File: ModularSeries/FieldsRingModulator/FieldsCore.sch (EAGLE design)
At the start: 37 parts

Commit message: Fields added and various updates to designs
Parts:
- removed C3, C4: 220nF, rcl:C-EU050-025X075
- removed C5, C6, C8, C9: 100nF, rcl:C-EU050-025X075
- removed C7: 22pF, rcl:C-EU050-025X075
- removed GNDT: 4XWIREPAD, ElectricNoodleBox:4XWIREPAD
- removed H3, H4: MOUNT-HOLE3.2, holes:MOUNT-HOLE3.2
- removed HPVOL, MSTR: A100K, ElectricNoodleBox:2XWIREPAD
- removed HP_OUT, HP_OUT1: 3XWIREPAD, ElectricNoodleBox:3XWIREPAD
- removed IC2: (no value), ElectricNoodleBox:TL0X2DIL
- removed IN1, IN2, IN3, IN4: B100K, ElectricNoodleBox:1XWIREPAD
- removed R10, R9: 75Ω, rcl:R-EU_0207/10
- removed R11: 1K, rcl:R-EU_0207/10
- removed R6, R7: 100K, rcl:R-EU_0207/10
- removed R8: 12K, rcl:R-EU_0207/10
- added CAR, IN, OUT: 1XWIREPAD, ElectricNoodleBox:1XWIREPAD
- added D1, D2, D3, D4: (no value), diode:DIODE-DO35-10
- added GND, POT: 2XWIREPAD, ElectricNoodleBox:2XWIREPAD
- added Z2: (no value), ElectricNoodleBox:Z1604_AUDIO_TRANSFORMER
- C1, C2: value 220nF -> 100nF
- H1, H2: value MOUNT-HOLE3.2 -> MOUNT-PAD-ROUND3.2; device holes:MOUNT-HOLE3.2 -> holes:MOUNT-PAD-ROUND3.2
- R1, R2, R3, R4: value 100K -> 10K
- R5: value 47K -> 100Ω
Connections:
- removed net HP_VOLOUT: HPVOL.2, IC2A.+IN, IC2B.+IN
- removed net N$15: HP_OUT1.1, Z1.6
- removed net N$16: HP_OUT1.2, Z1.5
- removed net N$17: HP_OUT1.3, Z1.4
- removed net N$18: IC2A.-IN, IC2A.OUT, R9.1
- removed net N$19: HP_OUT.1, R9.2
- removed net N$20: IC2B.-IN, IC2B.OUT, R10.1
- removed net N$21: HP_OUT.2, R10.2
- removed net N$22: R11.2, Z1.1
- removed net N$9: C2.2, R2.1
- net +12V: now also C1.1; no longer C5.1, C8.1, IC2P.V+
- net -12V: now also C2.2; no longer C6.2, C9.2, IC2P.V-
- net AGND: now also C1.2, C2.1, GND.1, GND.2, IC1A.+IN, Z2.3, Z2.5; no longer C5.2, C6.1, C8.2, C9.1, GNDT.1, GNDT.2, GNDT.3, GNDT.4, HP_OUT.3, R6.2
- net N$1: now also D1.A, D4.C, Z1.6; no longer C4.1, IN4.1
- net N$10: now also POT.1, R2.2; no longer C3.2, R3.1
- net N$11: now also IC1A.OUT, POT.2, R3.1; no longer C4.2, R4.1
- net N$12: now also IC1B.-IN, R3.2, R4.1; no longer C2.1, IN2.1
- net N$13: now also IC1B.OUT, R4.2, R5.1; no longer C1.1, IN1.1
- net N$14: now also OUT.1, R5.2; no longer MSTR.2, R11.1
- net N$2: now also D1.C, D2.A, Z2.6; no longer C7.1, IC1A.-IN, R1.2, R2.2, R3.2, R4.2, R5.2
- net N$3: now also D2.C, D3.A, Z1.4; no longer C7.2, IC1A.OUT, R5.1, R7.1
- net N$4: now also D3.C, D4.A, Z2.4; no longer IC1B.-IN, R7.2, R8.1
- net N$5: now also CAR.1, Z1.5; no longer HPVOL.1, IC1B.OUT, MSTR.1, R8.2
- net N$6: now also R1.1, Z2.1; no longer C3.1, IN3.1
- net N$7: now also IC1A.-IN, R1.2, R2.1; no longer IC1A.+IN, R6.1
- net N$8: now also IN.1, Z1.1; no longer C1.2, R1.1
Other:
- note added: "B100K"
- note added: "R1 and R2 might need to be higher e.g. 22K"
- note added: "Recommended 1N34, 1N270 or BAT85 for D1, 2, 3 and 4"
- note removed: "1 - In phase 2 - GND 3 - Out of phase Only use 3 for balanced output, use 1 and 2 only for unbalanced"
- note removed: "Endings: AC Mixer and Isolated Output Aidan Taylor 2020 ELECTRIC NOODLE BOX"
- note removed: "Headphone Driver to TRS Minijack"
- moved on the sheet: C1, C2, H1, H2, IC1A, IC1B, IC1P, R1, R2, R3, R4, R5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

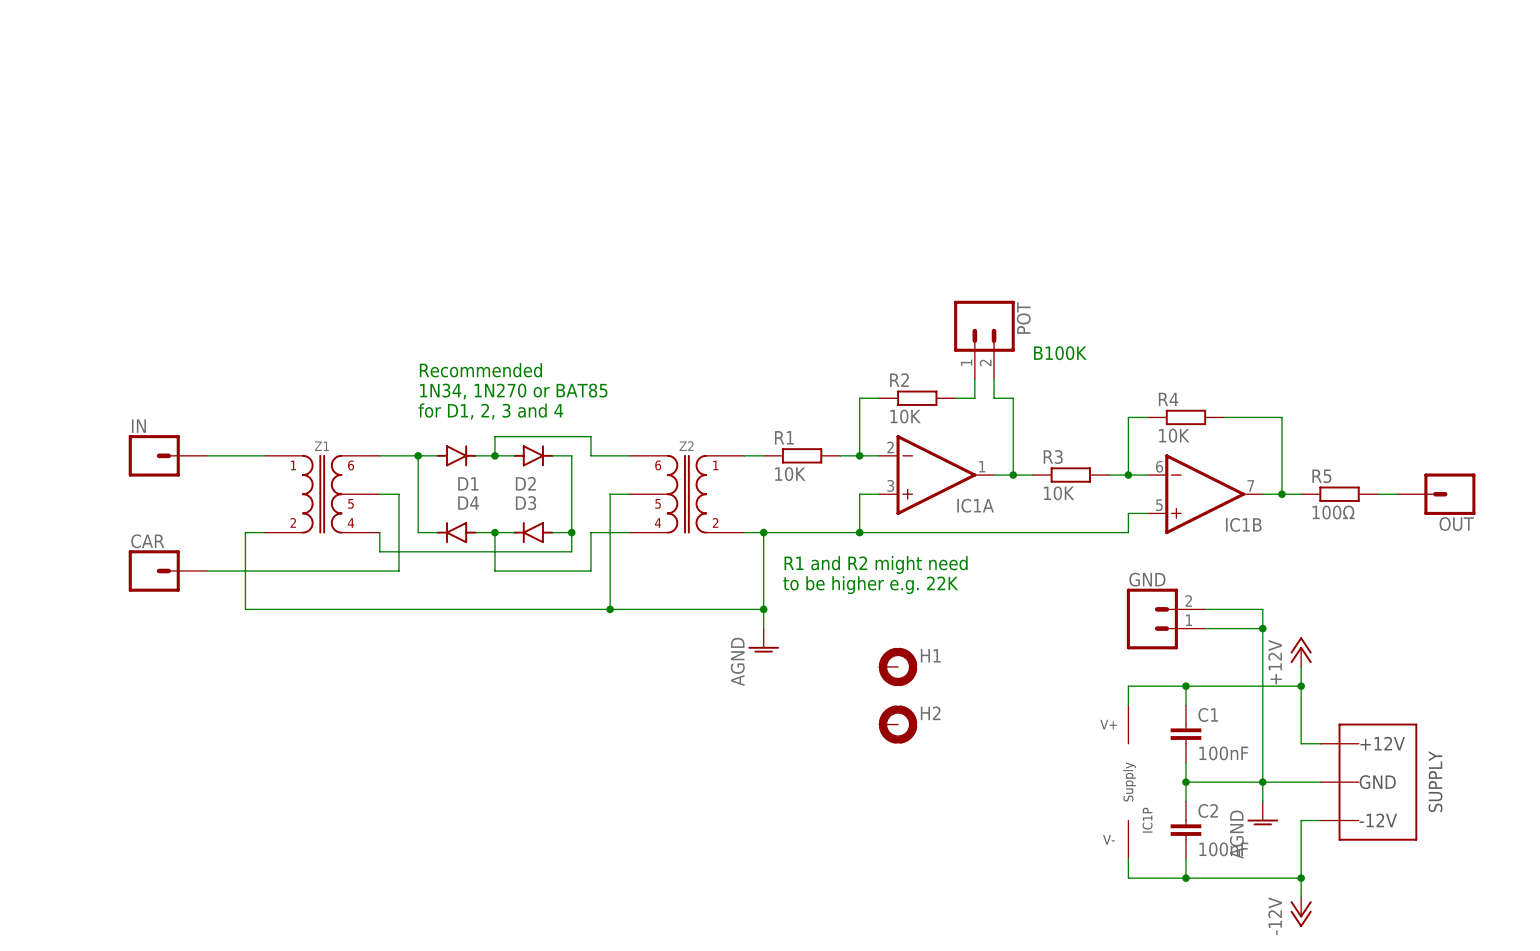
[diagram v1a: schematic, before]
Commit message: Fields module images and BOM added
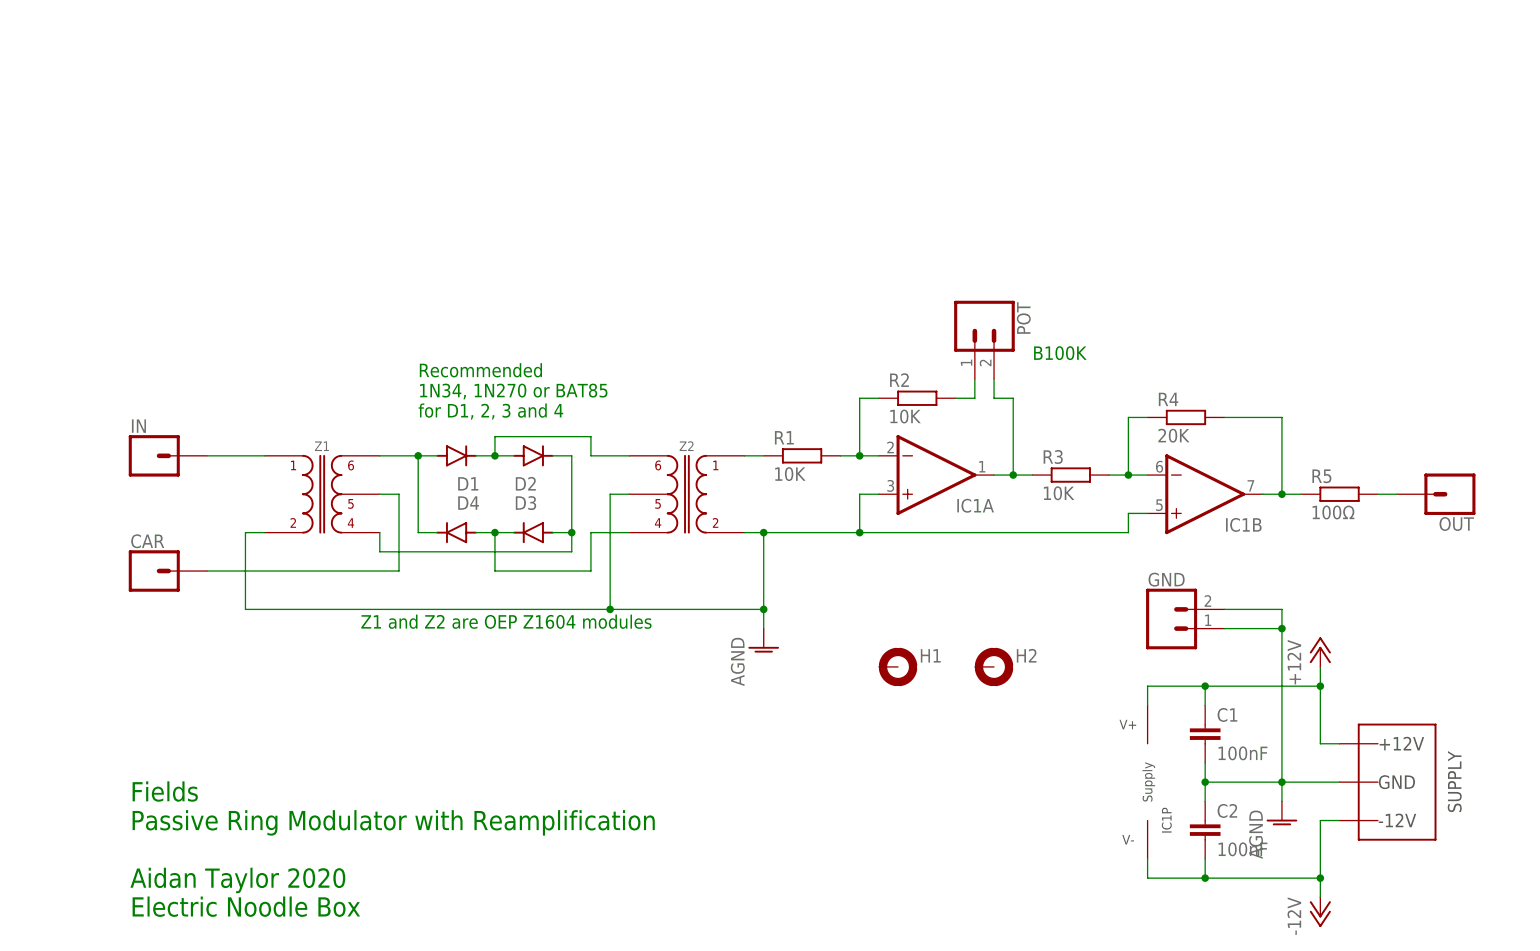
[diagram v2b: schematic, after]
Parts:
- R4: value 10K -> 20K
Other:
- note added: "Fields Passive Ring Modulator with Reamplification Aidan Taylor 2020 Electric Noodle Box"
- note added: "Z1 and Z2 are OEP Z1604 modules"
- note removed: "R1 and R2 might need to be higher e.g. 22K"
- moved on the sheet: C1, C2, GND, H2, IC1P
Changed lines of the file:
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@@
 <part name="POT" library="ElectricNoodleBox" deviceset="2XWIREPAD" device=""/>
 <part name="R3" library="rcl" library_urn="urn:adsk.eagle:library:334" deviceset="R-EU_" device="0207/10" package3d_urn="urn:adsk.eagle:package:23491/2" value="10K"/>
-<part name="R4" library="rcl" library_urn="urn:adsk.eagle:library:334" deviceset="R-EU_" device="0207/10" package3d_urn="urn:adsk.eagle:package:23491/2" value="10K"/>
+<part name="R4" library="rcl" library_urn="urn:adsk.eagle:library:334" deviceset="R-EU_" device="0207/10" package3d_urn="urn:adsk.eagle:package:23491/2" value="20K"/>
 <part name="R5" library="rcl" library_urn="urn:adsk.eagle:library:334" deviceset="R-EU_" device="0207/10" package3d_urn="urn:adsk.eagle:package:23491/2" value="100Ω"/>
 <part name="P+1" library="supply1" library_urn="urn:adsk.eagle:library:371" deviceset="+12V" device=""/>
@@
 1N34, 1N270 or BAT85
 for D1, 2, 3 and 4</text>
-<text x="93.98" y="38.1" size="1.778" layer="91">R1 and R2 might need
-to be higher e.g. 22K</text>
 <text x="127" y="68.58" size="1.778" layer="91">B100K </text>
+<text x="38.1" y="33.02" size="1.778" layer="91">Z1 and Z2 are OEP Z1604 modules</text>
+<text x="7.62" y="-5.08" size="2.54" layer="91">Fields
+Passive Ring Modulator with Reamplification
+Aidan Taylor 2020
+Electric Noodle Box</text>
 </plain>
 <instances>
@@
 <attribute name="NAME" x="152.4" y="47.625" size="1.778" layer="95" rot="MR180"/>
 </instance>
-<instance part="IC1" gate="P" x="139.7" y="12.7" smashed="yes">
-<attribute name="NAME" x="142.24" y="7.62" size="1.27" layer="97" rot="R90" align="center"/>
-</instance>
-<instance part="WP1" gate="G$1" x="172.72" y="12.7" smashed="yes"/>
+<instance part="IC1" gate="P" x="142.24" y="12.7" smashed="yes">
+<attribute name="NAME" x="144.78" y="7.62" size="1.27" layer="97" rot="R90" align="center"/>
+</instance>
+<instance part="WP1" gate="G$1" x="175.26" y="12.7" smashed="yes"/>
 <instance part="R1" gate="G$1" x="96.52" y="55.88" smashed="yes">
 <attribute name="NAME" x="92.71" y="57.3786" size="1.778" layer="95"/>
@@
 <attribute name="VALUE" x="163.83" y="47.498" size="1.778" layer="96"/>
 </instance>
-<instance part="P+1" gate="1" x="162.56" y="30.48" smashed="yes">
-<attribute name="VALUE" x="160.02" y="25.4" size="1.778" layer="96" rot="R90"/>
-</instance>
-<instance part="P-1" gate="1" x="162.56" y="-5.08" smashed="yes">
-<attribute name="VALUE" x="160.02" y="-7.62" size="1.778" layer="96" rot="R90"/>
-</instance>
-<instance part="AGND1" gate="VR1" x="157.48" y="7.62" smashed="yes">
-<attribute name="VALUE" x="154.94" y="2.54" size="1.778" layer="96" rot="R90"/>
-</instance>
-<instance part="C1" gate="G$1" x="147.32" y="20.32" smashed="yes">
-<attribute name="NAME" x="148.844" y="20.701" size="1.778" layer="95"/>
-<attribute name="VALUE" x="148.844" y="15.621" size="1.778" layer="96"/>
-</instance>
-<instance part="C2" gate="G$1" x="147.32" y="7.62" smashed="yes">
-<attribute name="NAME" x="148.844" y="8.001" size="1.778" layer="95"/>
-<attribute name="VALUE" x="148.844" y="2.921" size="1.778" layer="96"/>
+<instance part="P+1" gate="1" x="165.1" y="30.48" smashed="yes">
+<attribute name="VALUE" x="162.56" y="25.4" size="1.778" layer="96" rot="R90"/>
+</instance>
+<instance part="P-1" gate="1" x="165.1" y="-5.08" smashed="yes">
+<attribute name="VALUE" x="162.56" y="-7.62" size="1.778" layer="96" rot="R90"/>
+</instance>
+<instance part="AGND1" gate="VR1" x="160.02" y="7.62" smashed="yes">
+<attribute name="VALUE" x="157.48" y="2.54" size="1.778" layer="96" rot="R90"/>
+</instance>
+<instance part="C1" gate="G$1" x="149.86" y="20.32" smashed="yes">
+<attribute name="NAME" x="151.384" y="20.701" size="1.778" layer="95"/>
+<attribute name="VALUE" x="151.384" y="15.621" size="1.778" layer="96"/>
+</instance>
+<instance part="C2" gate="G$1" x="149.86" y="7.62" smashed="yes">
+<attribute name="NAME" x="151.384" y="8.001" size="1.778" layer="95"/>
+<attribute name="VALUE" x="151.384" y="2.921" size="1.778" layer="96"/>
 </instance>
 <instance part="H1" gate="G$1" x="109.22" y="27.94" smashed="yes">
 <attribute name="NAME" x="112.014" y="28.5242" size="1.778" layer="95"/>
 </instance>
-<instance part="H2" gate="G$1" x="109.22" y="20.32" smashed="yes">
-<attribute name="NAME" x="112.014" y="20.9042" size="1.778" layer="95"/>
+<instance part="H2" gate="G$1" x="121.92" y="27.94" smashed="yes">
+<attribute name="NAME" x="124.714" y="28.5242" size="1.778" layer="95"/>
 </instance>
 <instance part="AGND2" gate="VR1" x="91.44" y="30.48" smashed="yes">
 <attribute name="VALUE" x="88.9" y="25.4" size="1.778" layer="96" rot="R90"/>
 </instance>
-<instance part="GND" gate="G$1" x="142.24" y="33.02" smashed="yes">
-<attribute name="NAME" x="139.7" y="38.608" size="1.778" layer="95" font="vector"/>
+<instance part="GND" gate="G$1" x="144.78" y="33.02" smashed="yes">
+<attribute name="NAME" x="142.24" y="38.608" size="1.778" layer="95" font="vector"/>
 </instance>
 </instances>
@@
 <pinref part="P+1" gate="1" pin="+12V"/>
 <pinref part="WP1" gate="G$1" pin="V++"/>
-<wire x1="165.1" y1="17.78" x2="162.56" y2="17.78" width="0.1524" layer="91"/>
-<wire x1="162.56" y1="17.78" x2="162.56" y2="25.4" width="0.1524" layer="91"/>
+<wire x1="167.64" y1="17.78" x2="165.1" y2="17.78" width="0.1524" layer="91"/>
+<wire x1="165.1" y1="17.78" x2="165.1" y2="25.4" width="0.1524" layer="91"/>
 <pinref part="IC1" gate="P" pin="V+"/>
-<wire x1="162.56" y1="25.4" x2="162.56" y2="27.94" width="0.1524" layer="91"/>
-<wire x1="139.7" y1="22.86" x2="139.7" y2="25.4" width="0.1524" layer="91"/>
-<wire x1="139.7" y1="25.4" x2="147.32" y2="25.4" width="0.1524" layer="91"/>
-<junction x="162.56" y="25.4"/>
+<wire x1="165.1" y1="25.4" x2="165.1" y2="27.94" width="0.1524" layer="91"/>
+<wire x1="142.24" y1="22.86" x2="142.24" y2="25.4" width="0.1524" layer="91"/>
+<wire x1="142.24" y1="25.4" x2="149.86" y2="25.4" width="0.1524" layer="91"/>
+<junction x="165.1" y="25.4"/>
 <pinref part="C1" gate="G$1" pin="1"/>
-<wire x1="147.32" y1="25.4" x2="162.56" y2="25.4" width="0.1524" layer="91"/>
-<wire x1="147.32" y1="25.4" x2="147.32" y2="22.86" width="0.1524" layer="91"/>
-<junction x="147.32" y="25.4"/>
+<wire x1="149.86" y1="25.4" x2="165.1" y2="25.4" width="0.1524" layer="91"/>
+<wire x1="149.86" y1="25.4" x2="149.86" y2="22.86" width="0.1524" layer="91"/>
+<junction x="149.86" y="25.4"/>
 </segment>
 </net>
@@
 <segment>
 <pinref part="WP1" gate="G$1" pin="V--"/>
-<wire x1="165.1" y1="7.62" x2="162.56" y2="7.62" width="0.1524" layer="91"/>
+<wire x1="167.64" y1="7.62" x2="165.1" y2="7.62" width="0.1524" layer="91"/>
 <pinref part="P-1" gate="1" pin="-12V"/>
-<wire x1="162.56" y1="7.62" x2="162.56" y2="0" width="0.1524" layer="91"/>
+<wire x1="165.1" y1="7.62" x2="165.1" y2="0" width="0.1524" layer="91"/>
 <pinref part="IC1" gate="P" pin="V-"/>
-<wire x1="162.56" y1="0" x2="162.56" y2="-2.54" width="0.1524" layer="91"/>
-<wire x1="139.7" y1="2.54" x2="139.7" y2="0" width="0.1524" layer="91"/>
-<wire x1="139.7" y1="0" x2="147.32" y2="0" width="0.1524" layer="91"/>
-<junction x="162.56" y="0"/>
+<wire x1="165.1" y1="0" x2="165.1" y2="-2.54" width="0.1524" layer="91"/>
+<wire x1="142.24" y1="2.54" x2="142.24" y2="0" width="0.1524" layer="91"/>
+<wire x1="142.24" y1="0" x2="149.86" y2="0" width="0.1524" layer="91"/>
+<junction x="165.1" y="0"/>
 <pinref part="C2" gate="G$1" pin="2"/>
-<wire x1="147.32" y1="0" x2="162.56" y2="0" width="0.1524" layer="91"/>
-<wire x1="147.32" y1="2.54" x2="147.32" y2="0" width="0.1524" layer="91"/>
-<junction x="147.32" y="0"/>
+<wire x1="149.86" y1="0" x2="165.1" y2="0" width="0.1524" layer="91"/>
+<wire x1="149.86" y1="2.54" x2="149.86" y2="0" width="0.1524" layer="91"/>
+<junction x="149.86" y="0"/>
 </segment>
 </net>
@@
 <segment>
 <pinref part="WP1" gate="G$1" pin="AGND"/>
-<wire x1="165.1" y1="12.7" x2="157.48" y2="12.7" width="0.1524" layer="91"/>
+<wire x1="167.64" y1="12.7" x2="160.02" y2="12.7" width="0.1524" layer="91"/>
 <pinref part="AGND1" gate="VR1" pin="AGND"/>
-<wire x1="157.48" y1="12.7" x2="157.48" y2="10.16" width="0.1524" layer="91"/>
+<wire x1="160.02" y1="12.7" x2="160.02" y2="10.16" width="0.1524" layer="91"/>
 <pinref part="C1" gate="G$1" pin="2"/>
 <pinref part="C2" gate="G$1" pin="1"/>
-<wire x1="147.32" y1="15.24" x2="147.32" y2="12.7" width="0.1524" layer="91"/>
-<wire x1="147.32" y1="12.7" x2="147.32" y2="10.16" width="0.1524" layer="91"/>
-<wire x1="147.32" y1="12.7" x2="157.48" y2="12.7" width="0.1524" layer="91"/>
-<junction x="147.32" y="12.7"/>
-<junction x="157.48" y="12.7"/>
-<wire x1="157.48" y1="33.02" x2="157.48" y2="12.7" width="0.1524" layer="91"/>
+<wire x1="149.86" y1="15.24" x2="149.86" y2="12.7" width="0.1524" layer="91"/>
+<wire x1="149.86" y1="12.7" x2="149.86" y2="10.16" width="0.1524" layer="91"/>
+<wire x1="149.86" y1="12.7" x2="160.02" y2="12.7" width="0.1524" layer="91"/>
+<junction x="149.86" y="12.7"/>
+<junction x="160.02" y="12.7"/>
+<wire x1="160.02" y1="33.02" x2="160.02" y2="12.7" width="0.1524" layer="91"/>
 <pinref part="GND" gate="G$1" pin="2"/>
-<wire x1="149.86" y1="35.56" x2="157.48" y2="35.56" width="0.1524" layer="91"/>
-<wire x1="157.48" y1="35.56" x2="157.48" y2="33.02" width="0.1524" layer="91"/>
+<wire x1="152.4" y1="35.56" x2="160.02" y2="35.56" width="0.1524" layer="91"/>
+<wire x1="160.02" y1="35.56" x2="160.02" y2="33.02" width="0.1524" layer="91"/>
 <pinref part="GND" gate="G$1" pin="1"/>
-<wire x1="149.86" y1="33.02" x2="157.48" y2="33.02" width="0.1524" layer="91"/>
-<junction x="157.48" y="33.02"/>
-</segment>
-<segment>
+<wire x1="152.4" y1="33.02" x2="160.02" y2="33.02" width="0.1524" layer="91"/>
+<junction x="160.02" y="33.02"/>
+</segment>
+<segment>
